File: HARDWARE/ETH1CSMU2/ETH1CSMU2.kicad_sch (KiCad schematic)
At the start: 0 parts

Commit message: Software development
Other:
- sheet Control ports: added SIGN_SEL; removed SING_SEL
- sheet Frontend ports: added SIGN_SEL; removed SING_SEL
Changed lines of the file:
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@@
-      (effects (font (size 1.27 1.27)) (justify left))
-    )
-    (pin "SING_SEL" output (at 119.38 201.93 180)
       (effects (font (size 1.27 1.27)) (justify left))
     )
@@
     (pin "SR_DAT" input (at 156.21 176.53 0)
       (effects (font (size 1.27 1.27)) (justify right))
+    )
+    (pin "SIGN_SEL" output (at 119.38 201.93 180)
+      (effects (font (size 1.27 1.27)) (justify left))
     )
     (instances
@@
       (effects (font (size 1.27 1.27)) (justify left))
     )
-    (pin "SING_SEL" input (at 238.76 46.99 180)
+    (pin "SIGN_SEL" input (at 238.76 46.99 180)
       (effects (font (size 1.27 1.27)) (justify left))
     )

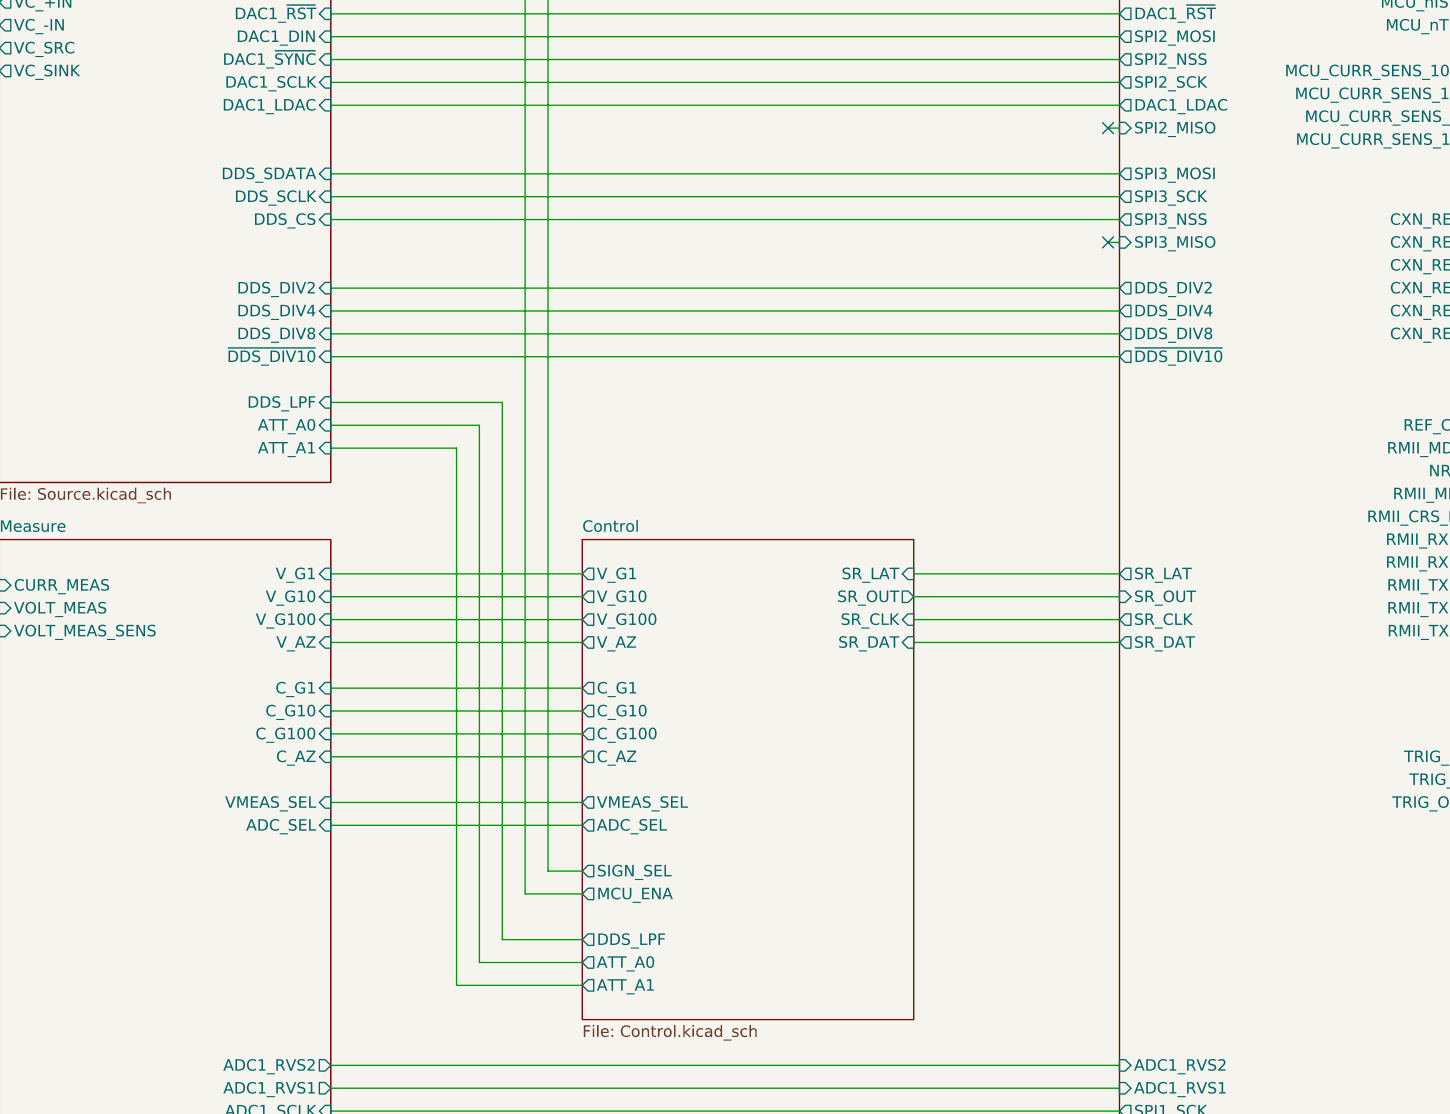
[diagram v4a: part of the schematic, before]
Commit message: Software development and hardware changes. FGEN code works.
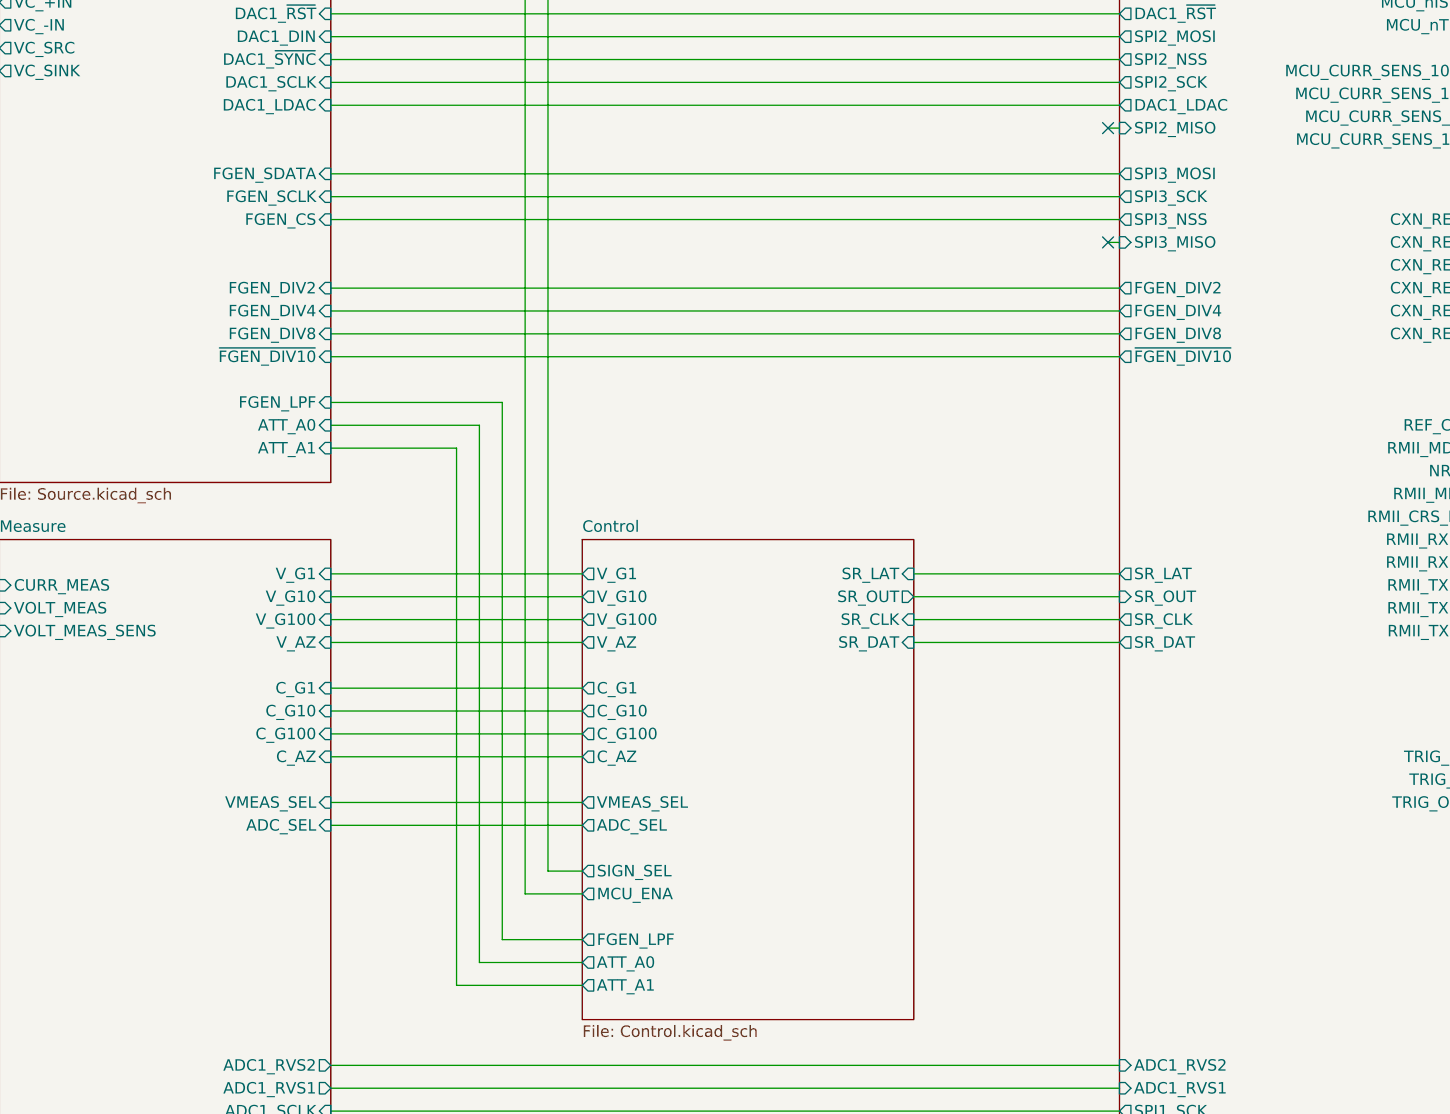
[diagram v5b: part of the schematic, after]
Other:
- sheet Control ports: added FGEN_LPF; removed DDS_LPF
- sheet MCU ports: added FGEN_DIV2, FGEN_DIV4, FGEN_DIV8, ~{FGEN_DIV10}; removed DDS_DIV2, DDS_DIV4, DDS_DIV8, ~{DDS_DIV10}
- sheet Source ports: added FGEN_CS, FGEN_DIV2, FGEN_DIV4, FGEN_DIV8, FGEN_LPF, FGEN_SCLK, FGEN_SDATA, ~{FGEN_DIV10}; removed DDS_CS, DDS_DIV2, DDS_DIV4, DDS_DIV8, DDS_LPF, DDS_SCLK, DDS_SDATA, ~{DDS_DIV10}
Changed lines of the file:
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@@
       (effects (font (size 1.27 1.27)) (justify left))
     )
-    (pin "~{DDS_DIV10}" output (at 179.07 144.78 180)
-      (effects (font (size 1.27 1.27)) (justify left))
-    )
-    (pin "DDS_DIV8" output (at 179.07 142.24 180)
-      (effects (font (size 1.27 1.27)) (justify left))
-    )
-    (pin "DDS_DIV4" output (at 179.07 139.7 180)
-      (effects (font (size 1.27 1.27)) (justify left))
-    )
-    (pin "DDS_DIV2" output (at 179.07 137.16 180)
+    (pin "~{FGEN_DIV10}" output (at 179.07 144.78 180)
+      (effects (font (size 1.27 1.27)) (justify left))
+    )
+    (pin "FGEN_DIV8" output (at 179.07 142.24 180)
+      (effects (font (size 1.27 1.27)) (justify left))
+    )
+    (pin "FGEN_DIV4" output (at 179.07 139.7 180)
+      (effects (font (size 1.27 1.27)) (justify left))
+    )
+    (pin "FGEN_DIV2" output (at 179.07 137.16 180)
       (effects (font (size 1.27 1.27)) (justify left))
     )
@@
       (effects (font (size 1.27 1.27)) (justify left))
     )
-    (pin "DDS_LPF" output (at 119.38 209.55 180)
+    (pin "FGEN_LPF" output (at 119.38 209.55 180)
       (effects (font (size 1.27 1.27)) (justify left))
     )
@@
       (effects (font (size 1.27 1.27)) (justify left))
     )
-    (pin "DDS_LPF" input (at 91.44 149.86 0)
+    (pin "FGEN_LPF" input (at 91.44 149.86 0)
       (effects (font (size 1.27 1.27)) (justify right))
     )
@@
       (effects (font (size 1.27 1.27)) (justify right))
     )
-    (pin "DDS_SDATA" input (at 91.44 124.46 0)
-      (effects (font (size 1.27 1.27)) (justify right))
-    )
-    (pin "DDS_SCLK" input (at 91.44 127 0)
-      (effects (font (size 1.27 1.27)) (justify right))
-    )
-    (pin "DDS_CS" input (at 91.44 129.54 0)
-      (effects (font (size 1.27 1.27)) (justify right))
-    )
-    (pin "DDS_DIV4" input (at 91.44 139.7 0)
-      (effects (font (size 1.27 1.27)) (justify right))
-    )
-    (pin "DDS_DIV8" input (at 91.44 142.24 0)
-      (effects (font (size 1.27 1.27)) (justify right))
-    )
-    (pin "DDS_DIV2" input (at 91.44 137.16 0)
-      (effects (font (size 1.27 1.27)) (justify right))
-    )
-    (pin "~{DDS_DIV10}" input (at 91.44 144.78 0)
-      (effects (font (size 1.27 1.27)) (justify right))
-    )
+    (pin "FGEN_SDATA" input (at 91.44 124.46 0)
+      (effects (font (size 1.27 1.27)) (justify right))
+    )
+    (pin "FGEN_SCLK" input (at 91.44 127 0)
+      (effects (font (size 1.27 1.27)) (justify right))
+    )
+    (pin "FGEN_CS" input (at 91.44 129.54 0)
+      (effects (font (size 1.27 1.27)) (justify right))
+    )
+    (pin "FGEN_DIV4" input (at 91.44 139.7 0)
+      (effects (font (size 1.27 1.27)) (justify right))
+    )
+    (pin "FGEN_DIV8" input (at 91.44 142.24 0)
+      (effects (font (size 1.27 1.27)) (justify right))
+    )
+    (pin "FGEN_DIV2" input (at 91.44 137.16 0)
+      (effects (font (size 1.27 1.27)) (justify right))
+    )
+    (pin "~{FGEN_DIV10}" input (at 91.44 144.78 0)
+      (effects (font (size 1.27 1.27)) (justify right))
+    )

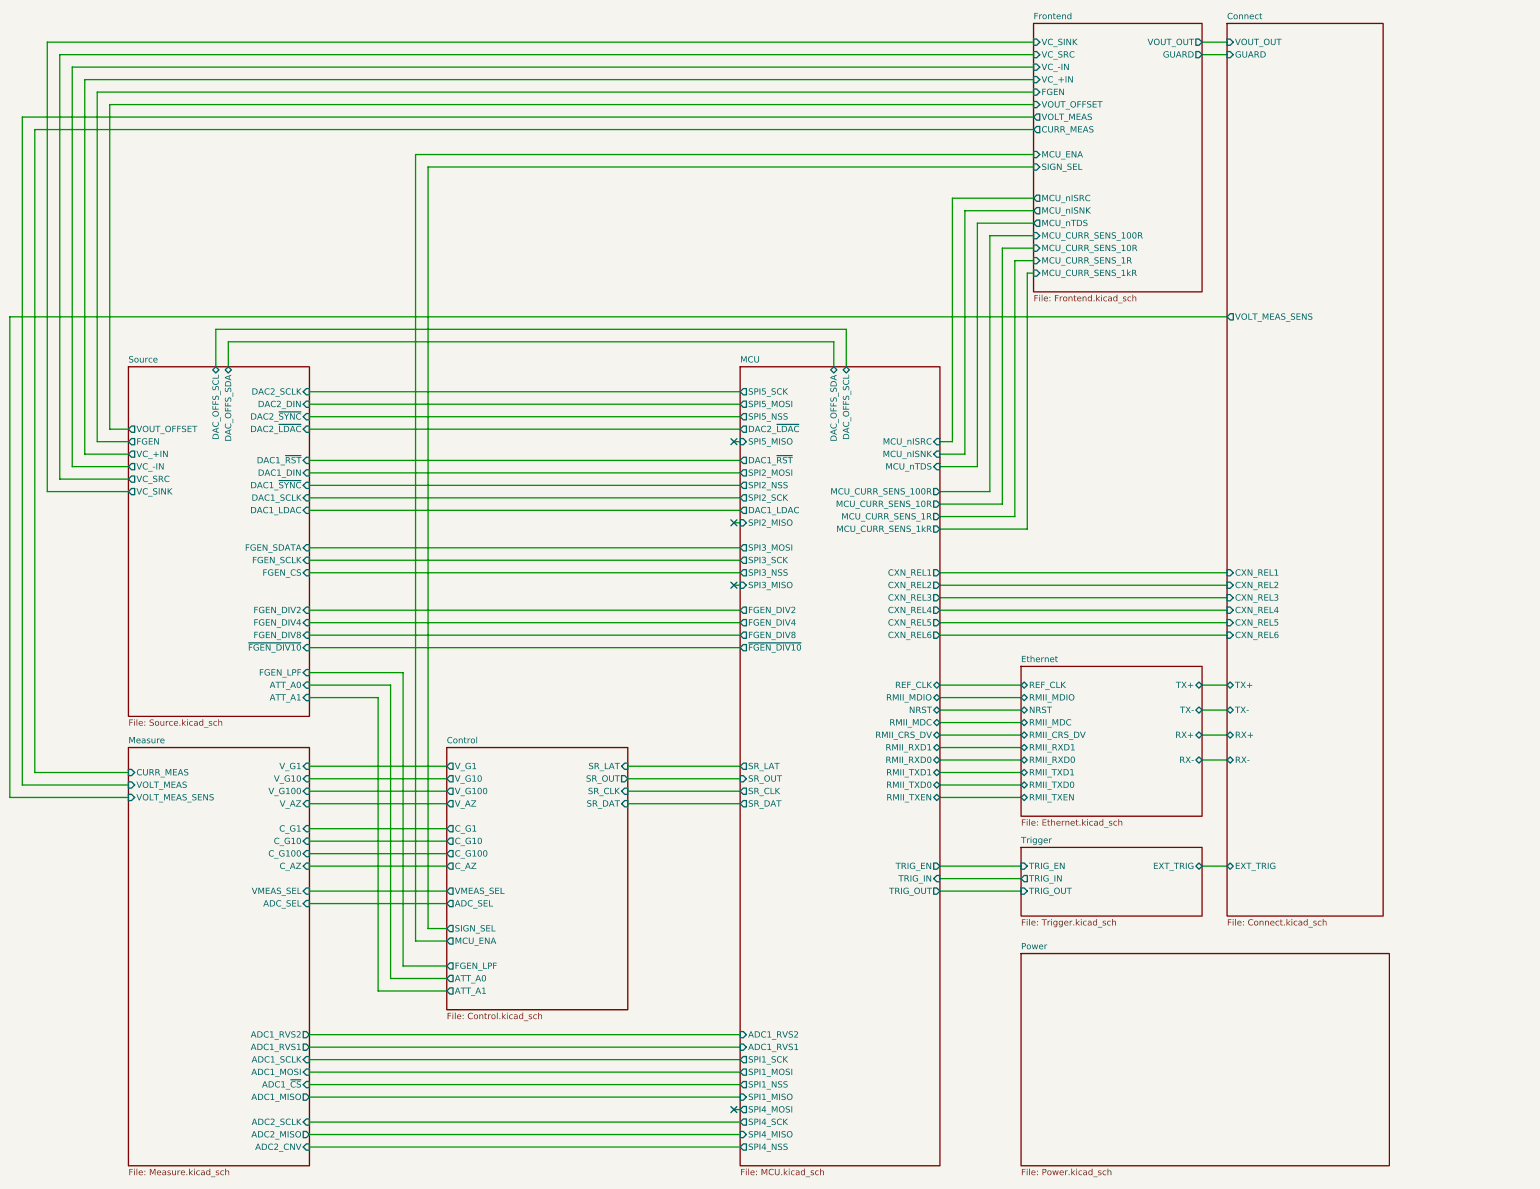
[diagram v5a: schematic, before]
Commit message: Hardware fix. Created README file
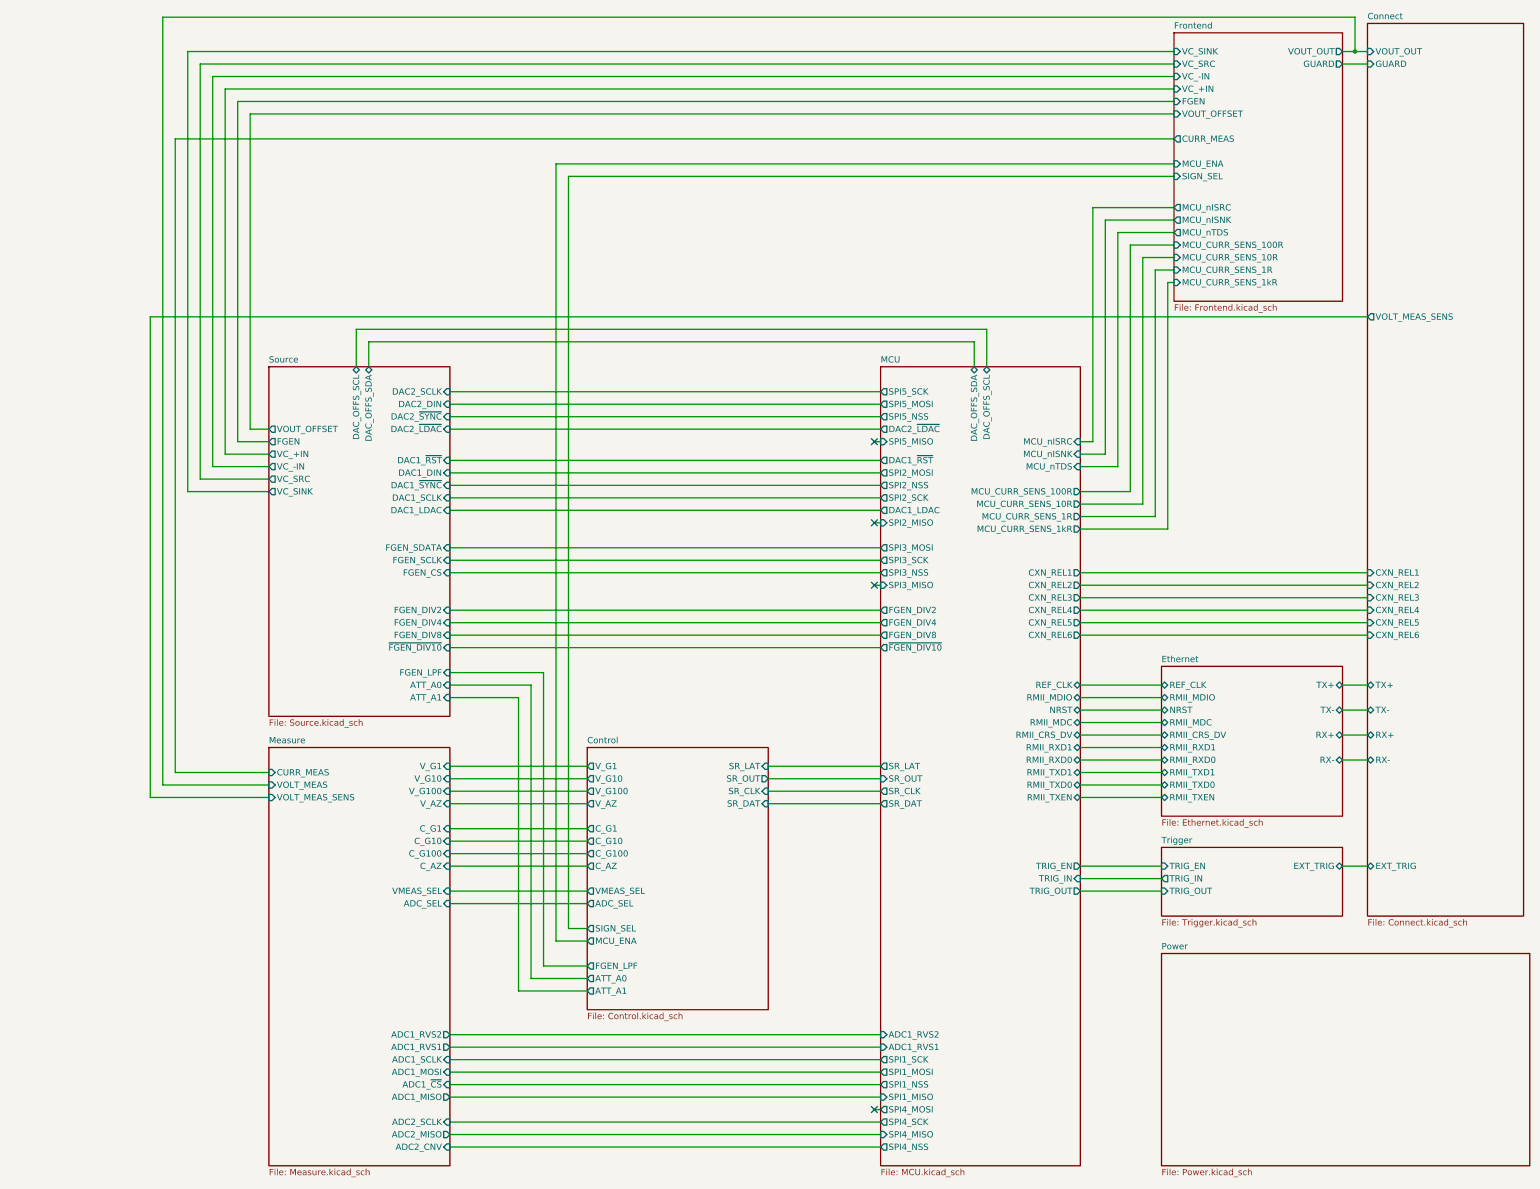
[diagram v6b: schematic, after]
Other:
- sheet Frontend ports: added none; removed VOLT_MEAS
- title: (none) -> ETH1CSMU2
